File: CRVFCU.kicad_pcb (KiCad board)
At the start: 4 copper layers, 50 x 100 mm, 151 parts, among them J1 TagConnect_TC2030, J3 USB_C_Receptacle_USB2.0_16P, J4 Micro_SD_Card_Det2, Q3 DMG2301L, Q4 BC818, Q5 DMG2301L, Q6 DMG2301L, SW1 SW_Omron_B3FS, SW2 SW_Nidec_CAS-120A1, U1 MS5611-01BA, U10 W25Q128JVS, U11 EClamp2515K, U12 ESDALC6V1W5, U13 USBLC6-2SC6, U14 USBLC6-2SC6, U15 MAX17049, U16 SI7232DN-T1, U17 SN74LV1T34DCK, U2 STM32H747IITx, U3 LIS2MDL, U4 ICM-45686, U5 FXMA108, U6 AP1117-50, U7 AP1117-33, U8 SI7232DN-T1, U9 USBLC6-4SC6, Y1 32.768khz, Y2 Crystal_GND24, Y3 32.768khz

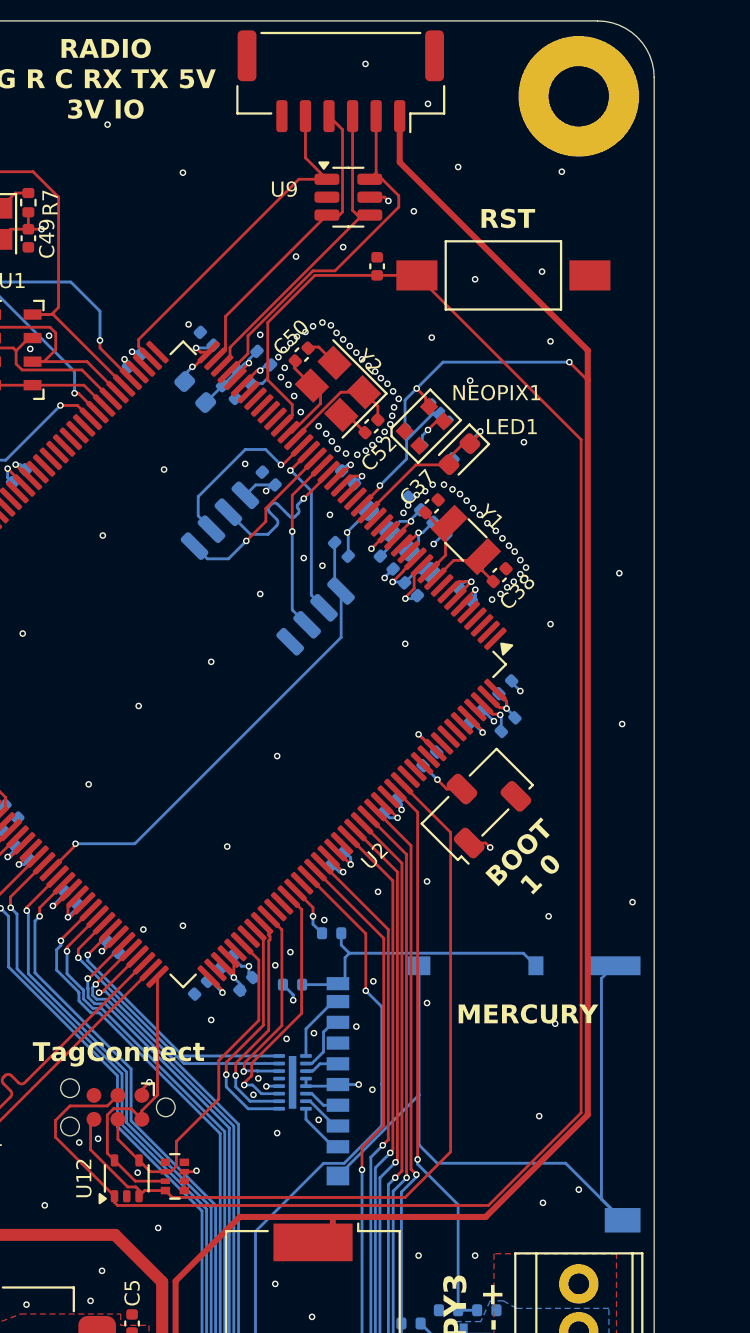
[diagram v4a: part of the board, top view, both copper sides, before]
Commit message: changed rst and boot to headers
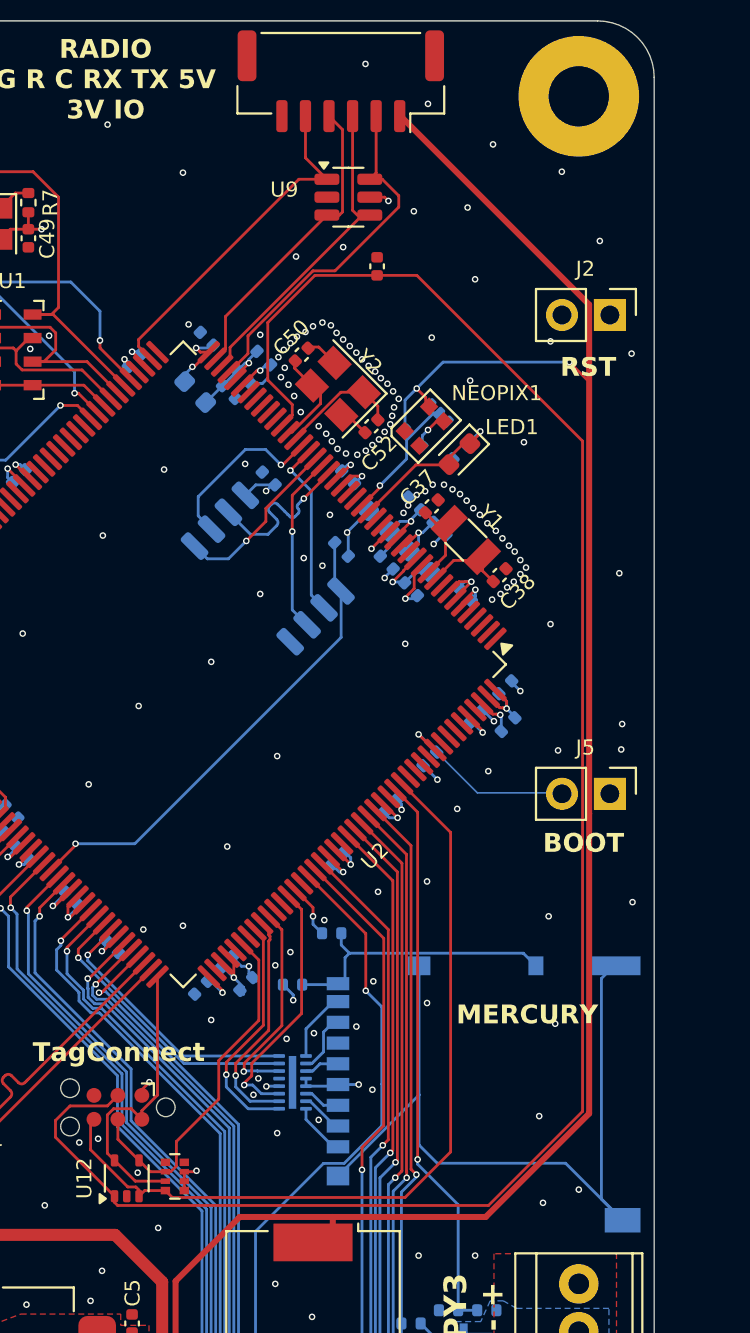
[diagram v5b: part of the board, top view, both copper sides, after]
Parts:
- removed SW1: SW_Omron_B3FS, Button_Switch_SMD:SW_SPST_FSMSM
- removed SW2: SW_Nidec_CAS-120A1, Button_Switch_SMD:Nidec_Copal_CAS-120A
- added J2: Conn_01x02, Connector_PinHeader_2.54mm:PinHeader_1x02_P2.54mm_Vertical, F.Cu at (87.7, 35.6)
- added J5: Conn_01x02, Connector_PinHeader_2.54mm:PinHeader_1x02_P2.54mm_Vertical, F.Cu at (87.7, 61.0)
- C37, C38: value 1.5pF -> 6pF
- C50, C52: value 3.9pF -> 10pF
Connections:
- R6 pad 2: Net-(SW2-B) -> GND
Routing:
- net Net-(J5-Pin_2): track 2.63 -> 10.2 mm
- net Net-(SW2-B): track 2.57 -> 0.00 mm, vias 1 -> 0
- net +3V3: track 89.3 -> 88.1 mm, vias 47 -> 46
- net GND: track 45.0 -> 46.1 mm, vias 212 -> 219
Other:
- board text added: "BOOT"
- board text removed: "BOOT 1 0"

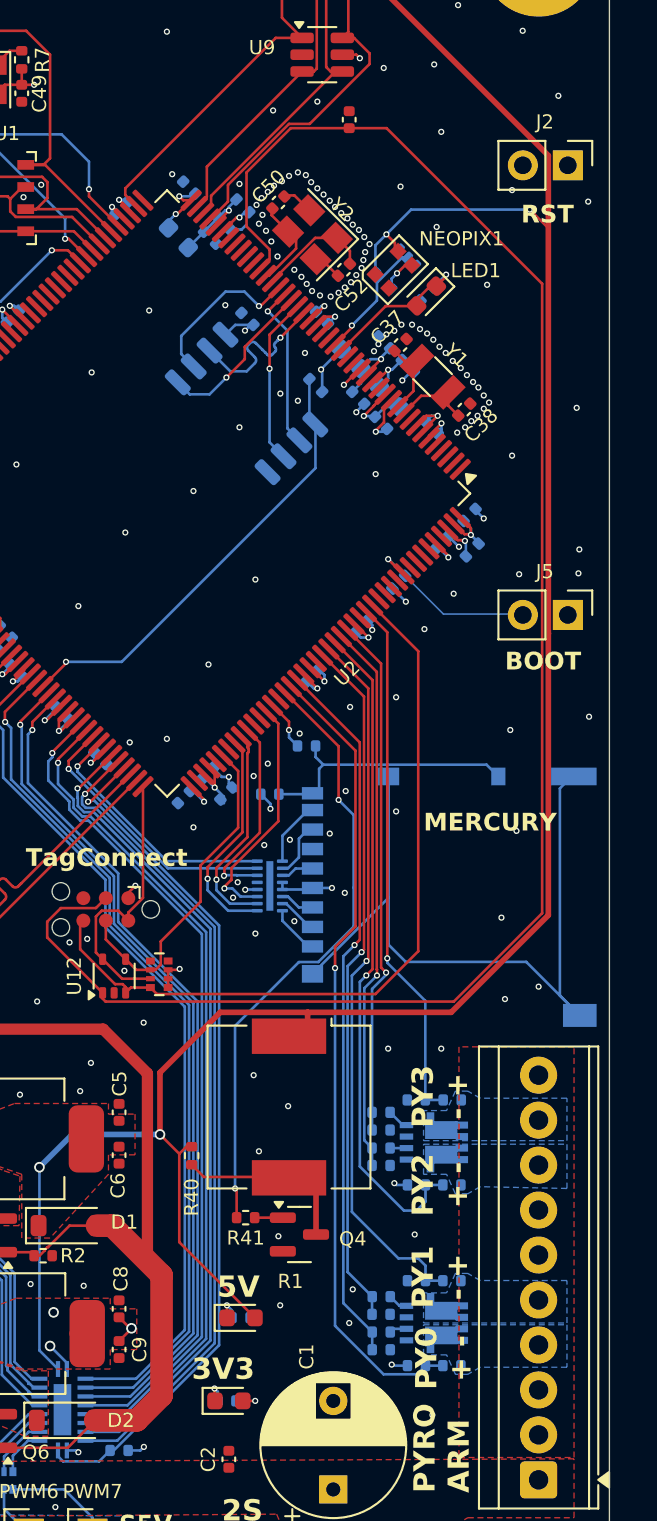
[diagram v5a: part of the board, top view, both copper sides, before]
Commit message: changed some small layout items and fixed drc
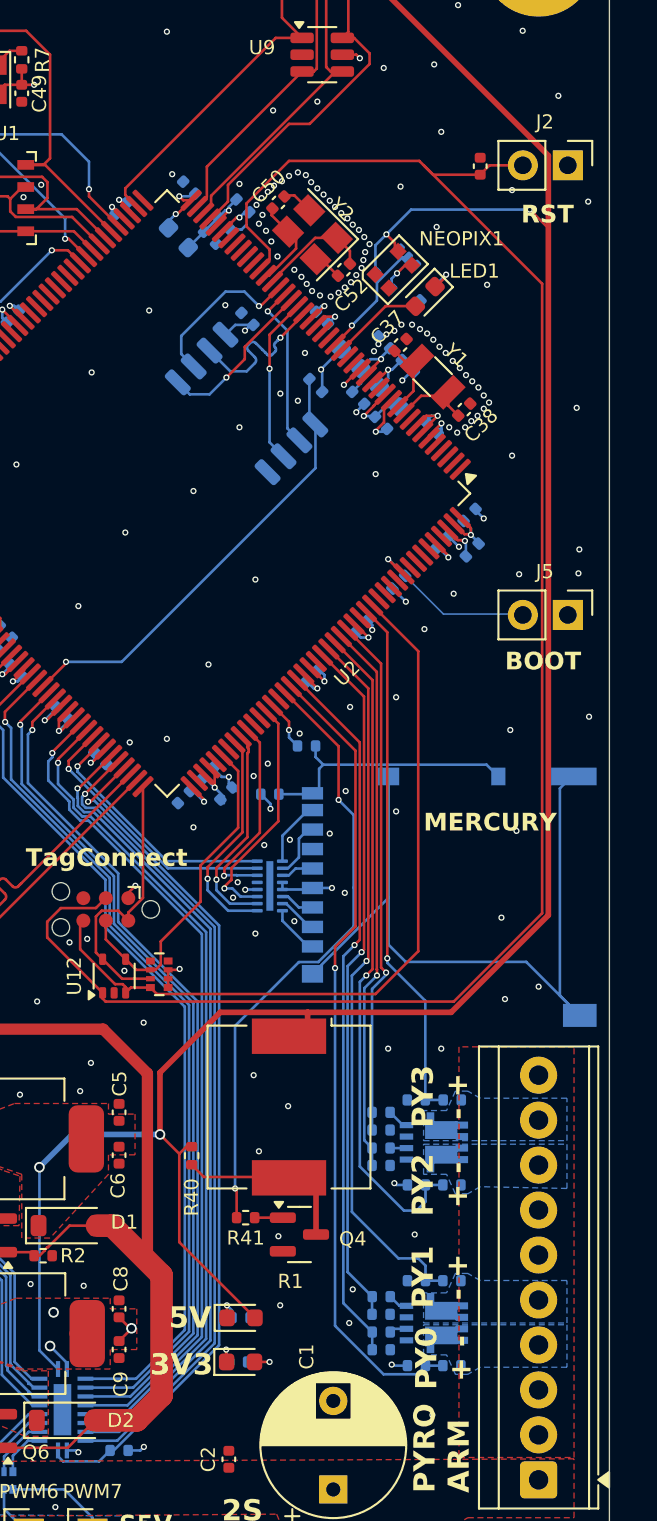
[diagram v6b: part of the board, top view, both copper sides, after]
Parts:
- moved C41 7.85 mm to (82.7, 35.6)
- moved 3V3_PWR1 2.30 mm to (69.2, 103.2)
- moved R37 2.30 mm to (69.0, 103.2)
- moved LED1 0.08 mm to (79.6, 43.0)
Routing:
- net /RESET: track 99.6 -> 103.1 mm
- net /LED: track 6.35 -> 4.93 mm
- net GND: vias 219 -> 220
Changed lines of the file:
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@@
 	(footprint "Capacitor_SMD:C_0402_1005Metric"
 		(layer "F.Cu")
-		(at 75.3 33.02 -90)
+		(at 82.7 35.65 -90)
 		(descr "Capacitor SMD 0402 (1005 Metric), square (rectangular) end terminal, IPC-7351 nominal, (Body size source: IPC-SM-782 page 76, https://www.pcb-3d.com/wordpress/wp-content/uploads/ipc-sm-782a_amendment_1_and_2.pdf), generated with kicad-footprint-generator")
 		(tags "capacitor")
@@
 		(tags "capacitor")
 		(property "Reference" "C9"
-			(at 0 -1.16 90)
+			(at 1.95 -0.1 90)
 			(layer "F.SilkS")
 			(effects
@@
 	(footprint "LED_SMD:LED_0603_1608Metric"
 		(layer "F.Cu")
-		(at 79.668153 42.981847 -135)
+		(at 79.593153 43.006847 -135)
 		(descr "LED SMD 0603 (1608 Metric), square (rectangular) end terminal, IPC-7351 nominal, (Body size source: http://www.tortai-tech.com/upload/download/2011102023233369053.pdf), generated with kicad-footprint-generator")
 		(tags "LED")
@@
 	(footprint "LED_SMD:LED_0603_1608Metric"
 		(layer "F.Cu")
-		(at 68.5025 105.4)
+		(at 69.1625 103.2)
 		(descr "LED SMD 0603 (1608 Metric), square (rectangular) end terminal, IPC-7351 nominal, (Body size source: http://www.tortai-tech.com/upload/download/2011102023233369053.pdf), generated with kicad-footprint-generator")
 		(tags "LED")
@@
 		(tags "resistor")
 		(property "Reference" "R46"
-			(at 0 1.17 0)
+			(at 2.459999 0 0)
 			(layer "B.SilkS")
 			(effects
@@
 	(footprint "Resistor_SMD:R_0402_1005Metric"
 		(layer "B.Cu")
-		(at 68.39 105.4)
+		(at 69.05 103.2)
 		(descr "Resistor SMD 0402 (1005 Metric), square (rectangular) end terminal, IPC-7351 nominal, (Body size source: IPC-SM-782 page 72, https://www.pcb-3d.com/wordpress/wp-content/uploads/ipc-sm-782a_amendment_1_and_2.pdf), generated with kicad-footprint-generator")
 		(tags "resistor")
@@
 		(tags "Micro SD")
 		(property "Reference" "J4"
-			(at -8.57 5.535 0)
+			(at -8.5 -2 0)
 			(layer "B.SilkS")
 			(effects
@@
 	)
 	(gr_text "3V3"
-		(at 66.4025 104.3 0)
+		(at 64.05 104.05 0)
 		(layer "F.SilkS")
 		(effects
@@
 	)
 	(gr_text "5V"
-		(at 67.8275 99.66 0)
+		(at 65.1 101.4 0)
 		(layer "F.SilkS")
 		(effects
@@
 	)
 	(segment
-		(start 67.69 104.7)
-		(end 67.69 105.375)
+		(start 68.35 102.5)
+		(end 68.35 103.175)
 		(width 0.15)
 		(layer "F.Cu")
@@
 	)
 	(segment
-		(start 67.69 105.375)
-		(end 67.715 105.4)
+		(start 68.35 103.175)
+		(end 68.375 103.2)
 		(width 0.15)
 		(layer "F.Cu")
@@
 	)
 	(via
-		(at 67.69 104.7)
+		(at 68.35 102.5)
 		(size 0.35)
 		(drill 0.2)
@@
 	)
 	(segment
-		(start 67.88 105.4)
-		(end 67.88 104.89)
+		(start 68.74 103.165)
+		(end 68.35 102.775)
 		(width 0.15)
 		(layer "B.Cu")
@@
 	)
 	(segment
-		(start 67.88 104.89)
-		(end 67.69 104.7)
+		(start 68.35 102.775)
+		(end 68.35 102.5)
 		(width 0.15)
 		(layer "B.Cu")
@@
 	)
 	(via
+		(at 80.95 50.4)
+		(size 0.35)
+		(drill 0.2)
+		(layers "F.Cu" "B.Cu")
+		(free yes)
+		(net 2)
+	)
+	(via
 		(at 75.7 41.8)
 		(size 0.35)
@@
 	)
 	(via
-		(at 82.296503 47.839748)
+		(at 82.25 47.8)
 		(size 0.35)
 		(drill 0.2)
@@
 	)
 	(via
-		(at 81.95 47.45)
+		(at 81.9 47.45)
 		(size 0.35)
 		(drill 0.2)
@@
 	)
 	(via
-		(at 81.6 47.05)
+		(at 81.55 47.05)
 		(size 0.35)
 		(drill 0.2)
@@
 	)
 	(segment
+		(start 69.95 103.2)
+		(end 70.8 103.2)
+		(width 0.15)
+		(layer "F.Cu")
+		(net 3)
+	)
+	(segment
 		(start 73.160691 44.289309)
 		(end 73.9 43.55)
@@
 	)
 	(segment
-		(start 69.29 105.4)
-		(end 69.99 105.4)
-		(width 0.15)
-		(layer "F.Cu")
-		(net 3)
-	)
-	(segment
 		(start 76.7 49.164214)
 		(end 77.332264 48.53195)
@@
 	)
 	(via
-		(at 69.99 105.4)
+		(at 70.8 103.2)
 		(size 0.35)
 		(drill 0.2)
@@
 	)
 	(segment
-		(start 68.012458 83.45)
-		(end 72.95 83.45)
+		(start 86.55 77.961034)
+		(end 86.55 35.05)
 		(width 0.32)
 		(layer "F.Cu")
@@
 	)
 	(segment
-		(start 72.95 83.45)
-		(end 72.95 84.35)
+		(start 68.012458 83.45)
+		(end 72.95 83.45)
 		(width 0.32)
 		(layer "F.Cu")
@@
 	(segment
 		(start 72.95 83.45)
-		(end 81.061034 83.45)
-		(width 0.32)
-		(layer "F.Cu")
-		(net 4)
-	)
-	(segment
-		(start 86.55 62.051)
-		(end 86.539 62.051)
+		(end 72.95 84.35)
 		(width 0.32)
 		(layer "F.Cu")
@@
 	)
 	(segment
-		(start 86.55 77.961034)
-		(end 86.55 62.051)
+		(start 72.95 83.45)
+		(end 81.061034 83.45)
 		(width 0.32)
 		(layer "F.Cu")
@@
 	)
 	(segment
-		(start 86.55 62.051)
-		(end 86.55 35.05)
-		(width 0.32)
-		(layer "F.Cu")
-		(net 4)
-	)
-	(segment
 		(start 66.099999 91.040001)
 		(end 65.7 91.44)
@@
 	)
 	(segment
-		(start 72 33.5)
-		(end 69.5 36)
+		(start 61.37 82.35)
+		(end 61.37 82.674999)
 		(width 0.15)
 		(layer "F.Cu")
@@
 	)
 	(segment
-		(start 61.37 82.35)
-		(end 61.37 82.674999)
+		(start 71.9 35.35)
+		(end 69.5 37.75)
 		(width 0.15)
 		(layer "F.Cu")
@@
 	)
 	(segment
-		(start 81.209 82.841)
-		(end 86.2 77.85)
+		(start 79.53 35.62)
+		(end 79.26 35.35)
 		(width 0.15)
 		(layer "F.Cu")
@@
 	)
 	(segment
-		(start 70.8 40.922079)
-		(end 70.261197 41.460882)
+		(start 58.2387 79.2187)
+		(end 61.37 82.35)
 		(width 0.15)
 		(layer "F.Cu")
@@
 	)
 	(segment
-		(start 58.2387 79.2187)
-		(end 61.37 82.35)
+		(start 70.8 40.922079)
+		(end 70.261197 41.460882)
 		(width 0.15)
 		(layer "F.Cu")
@@
 	)
 	(segment
-		(start 59.010517 77.5597)
-		(end 58.2387 78.331517)
+		(start 82.7 36.13)
+		(end 80.04 36.13)
 		(width 0.15)
 		(layer "F.Cu")
@@
 	)
 	(segment
-		(start 86.2 42.29)
-		(end 77.41 33.5)
+		(start 59.010517 77.5597)
+		(end 58.2387 78.331517)
 		(width 0.15)
 		(layer "F.Cu")
@@
 	)
 	(segment
-		(start 61.37 82.674999)
-		(end 61.536001 82.841)
+		(start 69.5 39.05)
+		(end 70.8 40.35)
 		(width 0.15)
 		(layer "F.Cu")
@@
 	)
 	(segment
-		(start 86.2 77.85)
-		(end 86.2 42.29)
+		(start 61.536001 82.841)
+		(end 81.209 82.841)
 		(width 0.15)
 		(layer "F.Cu")
@@
 	)
 	(segment
-		(start 69.5 36)
-		(end 69.5 39.05)
+		(start 86.2 42.29)
+		(end 79.53 35.62)
 		(width 0.15)
 		(layer "F.Cu")
@@
 	)
 	(segment
-		(start 61.536001 82.841)
-		(end 81.209 82.841)
+		(start 86.2 77.85)
+		(end 86.2 42.29)
 		(width 0.15)
 		(layer "F.Cu")
@@
 	)
 	(segment
-		(start 77.41 33.5)
-		(end 72 33.5)
+		(start 85.11 35.6)
+		(end 83.23 35.6)
 		(width 0.15)
 		(layer "F.Cu")
@@
 	)
 	(segment
-		(start 69.5 39.05)
-		(end 70.8 40.35)
+		(start 61.37 82.674999)
+		(end 61.536001 82.841)
+		(width 0.15)
+		(layer "F.Cu")
+		(net 23)
+	)
+	(segment
+		(start 80.04 36.13)
+		(end 79.53 35.62)
 		(width 0.15)
 		(layer "F.Cu")
@@
 	)
 	(segment
+		(start 81.209 82.841)
+		(end 86.2 77.85)
+		(width 0.15)
+		(layer "F.Cu")
+		(net 23)
+	)
+	(segment
+		(start 83.23 35.6)
+		(end 82.7 36.13)
+		(width 0.15)
+		(layer "F.Cu")
+		(net 23)
+	)
+	(segment
+		(start 79.26 35.35)
+		(end 71.9 35.35)
+		(width 0.15)
+		(layer "F.Cu")
+		(net 23)
+	)
+	(segment
+		(start 69.5 37.75)
+		(end 69.5 39.05)
+		(width 0.15)
+		(layer "F.Cu")
+		(net 23)
+	)
+	(segment
 		(start 48.13 40.65)
 		(end 48.2175 40.5625)
@@
 		(width 0.15)
 		(layer "F.Cu")
-		(net 48)
-	)
-	(segment
-		(start 78.748438 43.551562)
-		(end 79.750682 42.549318)
-		(width 0.15)
-		(layer "F.Cu")

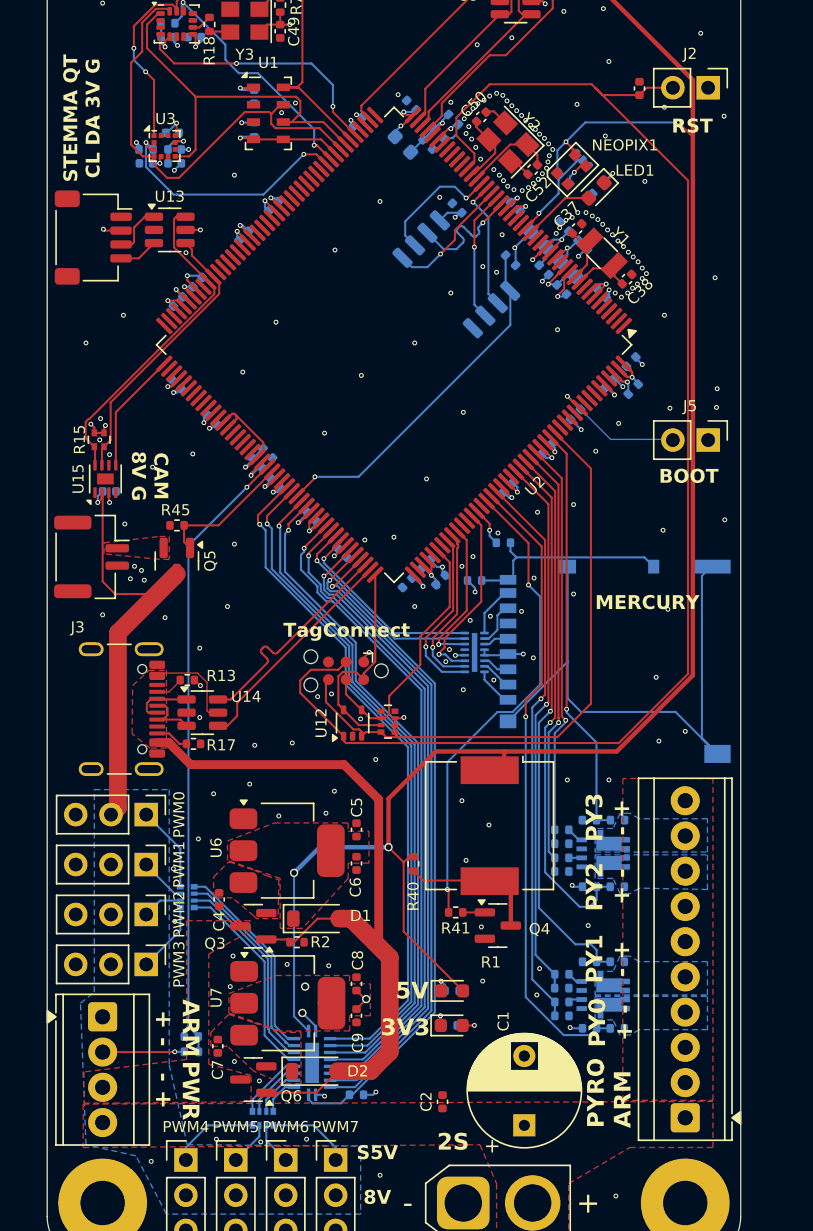
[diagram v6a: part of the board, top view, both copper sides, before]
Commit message: made oscillator vias more standardized
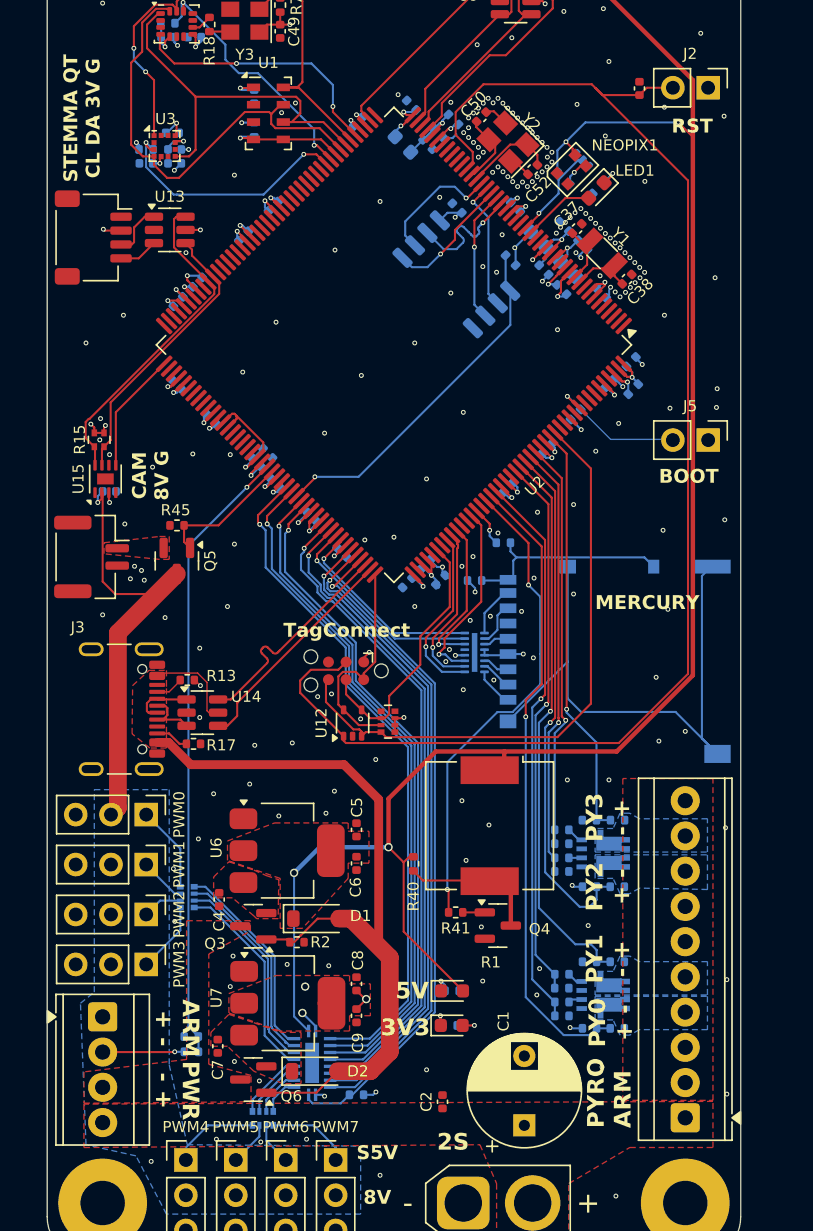
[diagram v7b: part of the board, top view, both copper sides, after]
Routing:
- net GND: track 46.1 -> 45.1 mm, vias 220 -> 230
